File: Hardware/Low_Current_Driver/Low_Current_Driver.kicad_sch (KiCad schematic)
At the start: 3 parts, among them J1 Conn_01x02_Socket, J2 Conn_01x02_Socket, J3 Screw_Terminal_01x04

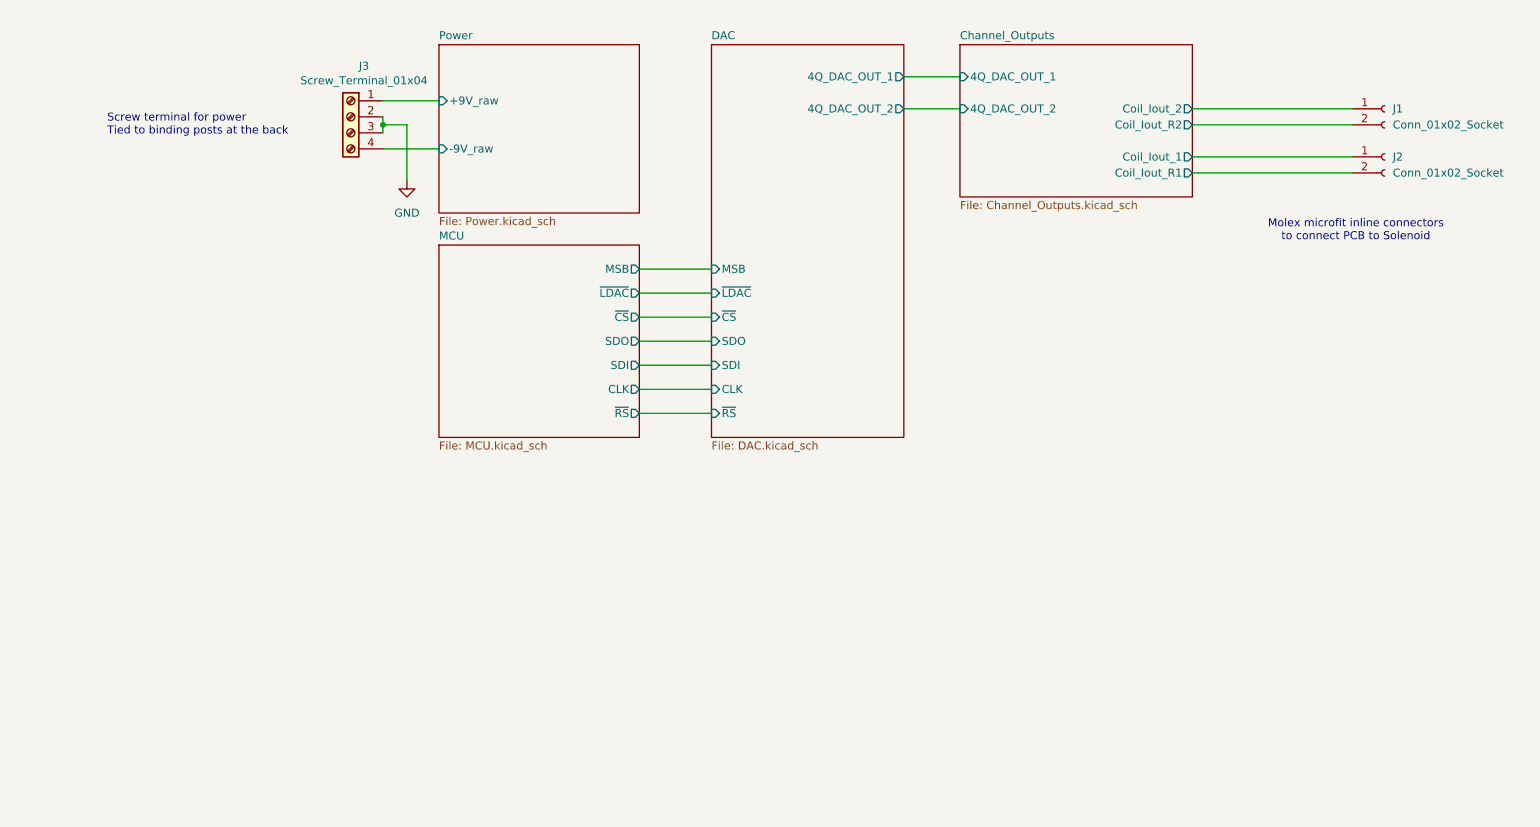
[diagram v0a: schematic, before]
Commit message: Replicate coil drive channel via native multichannel sheets
Root schematic now instantiates Channel_Outputs.kicad_sch twice as
Coil_Drive_A / Coil_Drive_B, with DAC_OPA.kicad_sch added as a sub-sheet
of DAC.kicad_sch (also instantiated twice). PCB relaid out to match.

Also drops the abandoned ESP32-S3 leftovers (footprint file and the
sym-lib-table entry pointing at an absolute path), removes the stale
Low_Current_Driver-cache legacy lib entry, and adds the STEP models
referenced by the board under 3DModels/.

Co-Authored-By: Claude Opus 4.8 <noreply@anthropic.com>
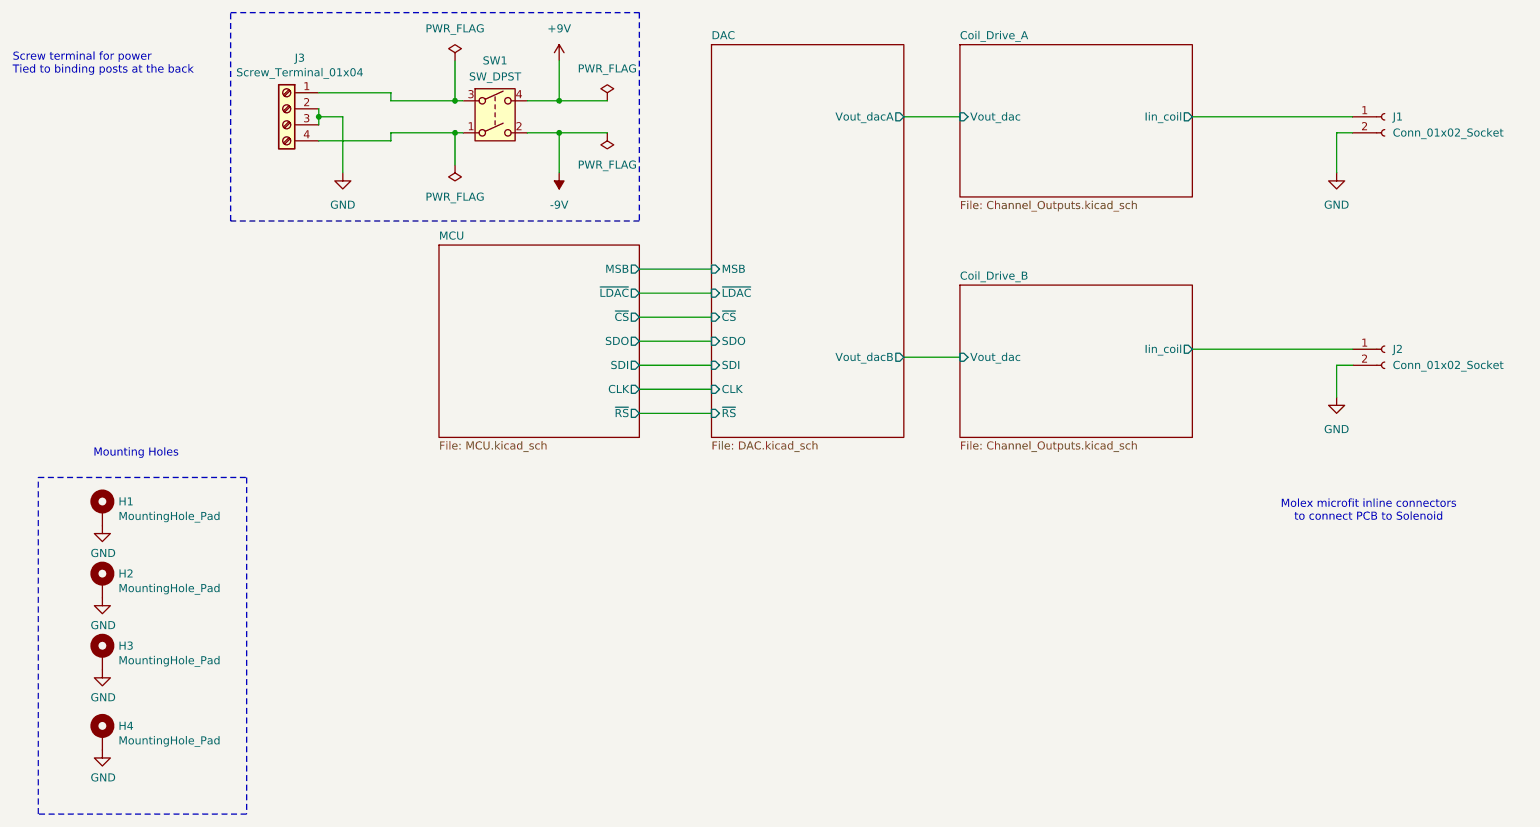
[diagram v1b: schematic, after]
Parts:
- added H1, H2, H3, H4: MountingHole_Pad, MountingHole:MountingHole_2.2mm_M2_DIN965_Pad, symbol Mechanical:MountingHole_Pad
- added SW1: SW_DPST, fieldZero:DPST_RA83231100, symbol Switch:SW_DPST
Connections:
- net Coil_Drive_A/Coil_Iout_R1 is gone; now on net GND: J2.2 (Pin_2)
- net Coil_Drive_A/Coil_Iout_R2 is gone; now on net GND: J1.2 (Pin_2)
- net GND: now also H1.1, H2.1, H3.1, H4.1
- net Coil_Drive_A/Coil_Iout_1 renamed Coil_Drive_B/Iin_coil
- net Coil_Drive_A/Coil_Iout_2 renamed Coil_Drive_A/Iin_coil
- net Power/+9V_raw: no longer names the net of J3.1 (Pin_1)
- net Power/+9V_raw: now also SW1.3
- net Power/-9V_raw: no longer names the net of J3.4 (Pin_4)
- net Power/-9V_raw: now also SW1.1
- new net +9V: SW1.4
- new net -9V: SW1.2
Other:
- sheet Channel_Outputs renamed Coil_Drive_A
- removed sheet Power
- added sheet Coil_Drive_B (Channel_Outputs.kicad_sch)
- sheet Coil_Drive_A ports: added Iin_coil, Vout_dac; removed 4Q_DAC_OUT_1, 4Q_DAC_OUT_2, Coil_Iout_1, Coil_Iout_2, Coil_Iout_R1, Coil_Iout_R2
- sheet DAC ports: added Vout_dacA, Vout_dacB; removed 4Q_DAC_OUT_1, 4Q_DAC_OUT_2
- note added: "Mounting Holes"
- company: Strathclyde University -> QUBIC MEG Lab
- title: "Vernier" Low Current Driver - LCD -> FieldZero Coil Driver - Low Current Driver (2 ch, +/-10 mA)
- moved on the sheet: J1, J2, J3
